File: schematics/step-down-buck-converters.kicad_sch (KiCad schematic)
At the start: 17 parts, among them U1 TPS54308, U3 TPS62203DBVTG4

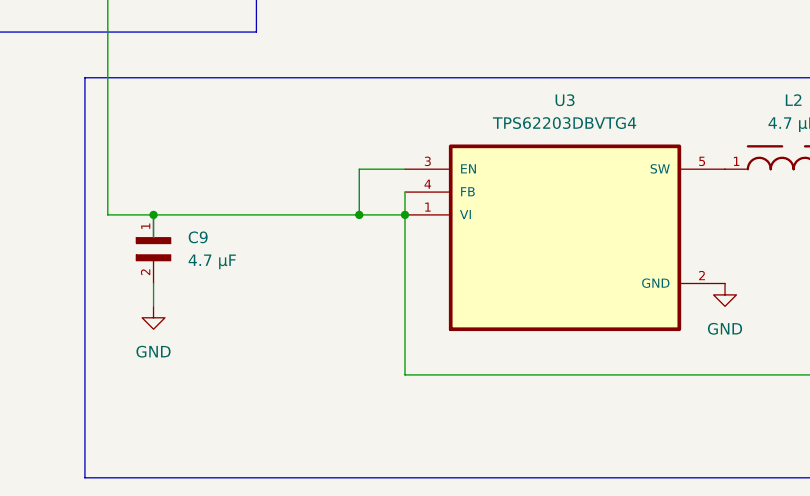
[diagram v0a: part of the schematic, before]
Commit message: I2C fixes (level shifter, pull-up resistors); short-circuit typo fix
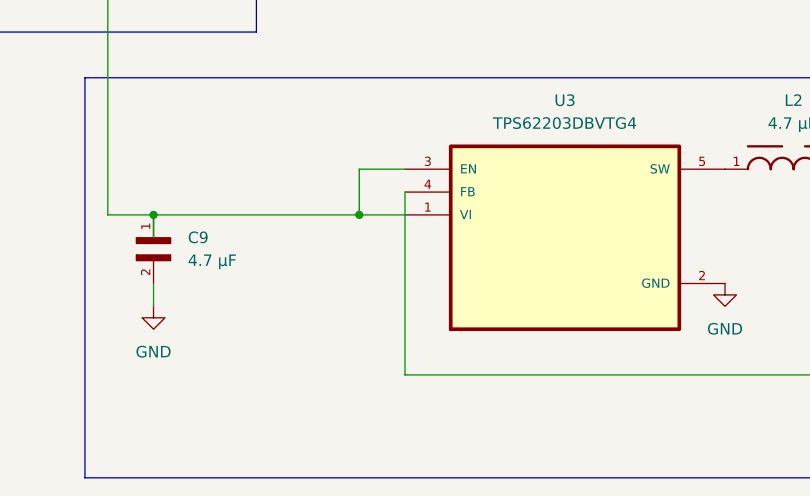
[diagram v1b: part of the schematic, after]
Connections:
- net 3V3: no longer C5.1, C6.1, C7.1, C9.1, L1.2, R1.1, R3.1, U3.1 (VI), U3.3 (EN)
- new net 5V: C5.1, C6.1, C7.1, C9.1, L1.2, R1.1, R3.1, U3.1 (VI), U3.3 (EN)
